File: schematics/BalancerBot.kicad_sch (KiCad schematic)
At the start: 7 parts, among them M1 Motor_DC, M2 Motor_DC, U1 MCP73871, U2 L298N

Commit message: Update
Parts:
- removed U2: L298N, Package_TO_SOT_THT:TO-220-15_P2.54x5.08mm_StaggerOdd_Lead4.58mm_Vertical, symbol Driver_Motor:L298N
- added Boost_5V: (no value), symbol 1MyLibrary:Power_Boost_module_-_5V_0.5A_JST
- added L9110S: (no value), symbol MyLibrary:L9110S
- added MPU6050: (no value), symbol 1MyLibrary:SEN-MPU6050
- renumbered U1 to BatteryManager
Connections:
- net at M2.1 (+): now also L9110S. (OUTA2)
- net at M2.2 (-): now also L9110S. (OUTA2)
- net at BatteryManager.14 (V_{BAT}), BatteryManager.15 (V_{BAT}): no longer BT1.1 (+)
- net at BT1.2 (-): now also Boost_5V. (Bat-)
- net at M1.1 (+): now also L9110S. (OUTA2)
- net at M1.2 (-): now also L9110S. (OUTA2)
- net GNDREF: now reaches A2.13 (GND), A2.18 (GND), A2.23 (GND), A2.28 (GND), A2.3 (GND), A2.38 (GND), A2.8 (GND)
- net GNDREF: now also Boost_5V. (Bat-), L9110S. (OUTA2), MPU6050. (GND)
- net at A2.21 (GPIO16): now also L9110S. (OUTA2)
- net at A2.22 (GPIO17): now also L9110S. (OUTA2)
- net at A2.24 (GPIO18): now also L9110S. (OUTA2)
- net at A2.25 (GPIO19): now also L9110S. (OUTA2)
- net at A2.26 (GPIO20): now also MPU6050. (GND)
- net at A2.27 (GPIO21): now also MPU6050. (GND)
- net at A2.36 (3V3): now also MPU6050. (GND)
- net at A2.39 (VSYS): now also Boost_5V. (Bat-), L9110S. (OUTA2)
- new net: BT1.1 (+), Boost_5V. (Bat-)
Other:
- note added: "ESP32 VIN = 6V/7.5V MOTORS(Vss) = 6V/7.5V RaspPico VSYS = 1.8-5.5V DC (no USB)"
- note added: "VBUS and VSYS must NOT be used simultaneously!"
- moved on the sheet: A1, A2, BT1, BatteryManager, M1, M2

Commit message: Update schematic
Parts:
- removed A1: Arduino_Nano_ESP32, Module:Arduino_Nano, symbol MCU_Module:Arduino_Nano_ESP32
- removed BatteryManager: MCP73871, Package_DFN_QFN:QFN-20-1EP_4x4mm_P0.5mm_EP2.5x2.5mm, symbol Battery_Management:MCP73871
- removed Boost_5V: (no value), symbol 1MyLibrary:Power_Boost_module_-_5V_0.5A_JST
- removed L9110S: (no value), symbol MyLibrary:L9110S
- removed M1, M2: Motor_DC, symbol Motor:Motor_DC
- added LED: Red, PCM_SparkFun-LED:LED_0402_1005Metric_Red, symbol PCM_SparkFun-LED:LED_Red_0402
- added M1, M2: Motor_Servo, symbol Motor:Motor_Servo
- added R1: 100ohm, symbol PCM_Resistor_AKL:R_Generic
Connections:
- net at MPU6050. (GND): now also A2.36 (3V3)
- net at BT1.1 (+): now also A2.39 (VSYS), M1.2 (+), M2.2 (+)
- net at BT1.2 (-): now also A2.13 (GND), A2.18 (GND), A2.23 (GND), A2.28 (GND), A2.3 (GND), A2.38 (GND), A2.8 (GND), MPU6050. (GND), LED.1 (K), M1.3 (-), M2.3 (-)
- net at A2.29 (GPIO22): now also R1.2
- net at A2.31 (GPIO26_ADC0): now also M1.1 (PWM)
- net at A2.32 (GPIO27_ADC1): now also M2.1 (PWM)
- removed net GNDREF: A2.13 (GND), A2.18 (GND), A2.23 (GND), A2.28 (GND), A2.3 (GND), A2.38 (GND), A2.8 (GND), MPU6050. (GND)
- new net: LED.2 (A), R1.1
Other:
- note added: "RaspPico VSYS = 1.8-5.5V DC (no USB)"
- note removed: "ESP32 VIN = 6V/7.5V MOTORS(Vss) = 6V/7.5V RaspPico VSYS = 1.8-5.5V DC (no USB)"
- moved on the sheet: A2, BT1, MPU6050

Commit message: 9dof IMU testing
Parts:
- added BT2: LiPo_Cell, symbol Device:Battery_Cell
- added D1: LED(G), symbol Device:LED
- added M3, M4: Motor_Servo, symbol Motor:Motor_Servo
- added R2: 220/110ohm, symbol PCM_Resistor_AKL:R_Generic
- added R3: 330ohm, symbol PCM_Resistor_AKL:R_Generic
- added SW1: SW_SPDT, symbol Switch:SW_SPDT
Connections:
- net at MPU6050. (GND): now also A2.36 (3V3)
- new net: BT2.1 (+), SW1.3 (C)
- new net: D1.2 (A), R2.2
- new net M1: M4.1 (PWM)
- new net M2: M3.1 (PWM)
- new net Pico GND: BT2.2 (-), D1.1 (K), M3.3 (-), M4.3 (-)
- new net Pico VSYS: M3.2 (+), M4.2 (+), R2.1, R3.2, SW1.2 (B)
- new net Voltage Measure: R3.1

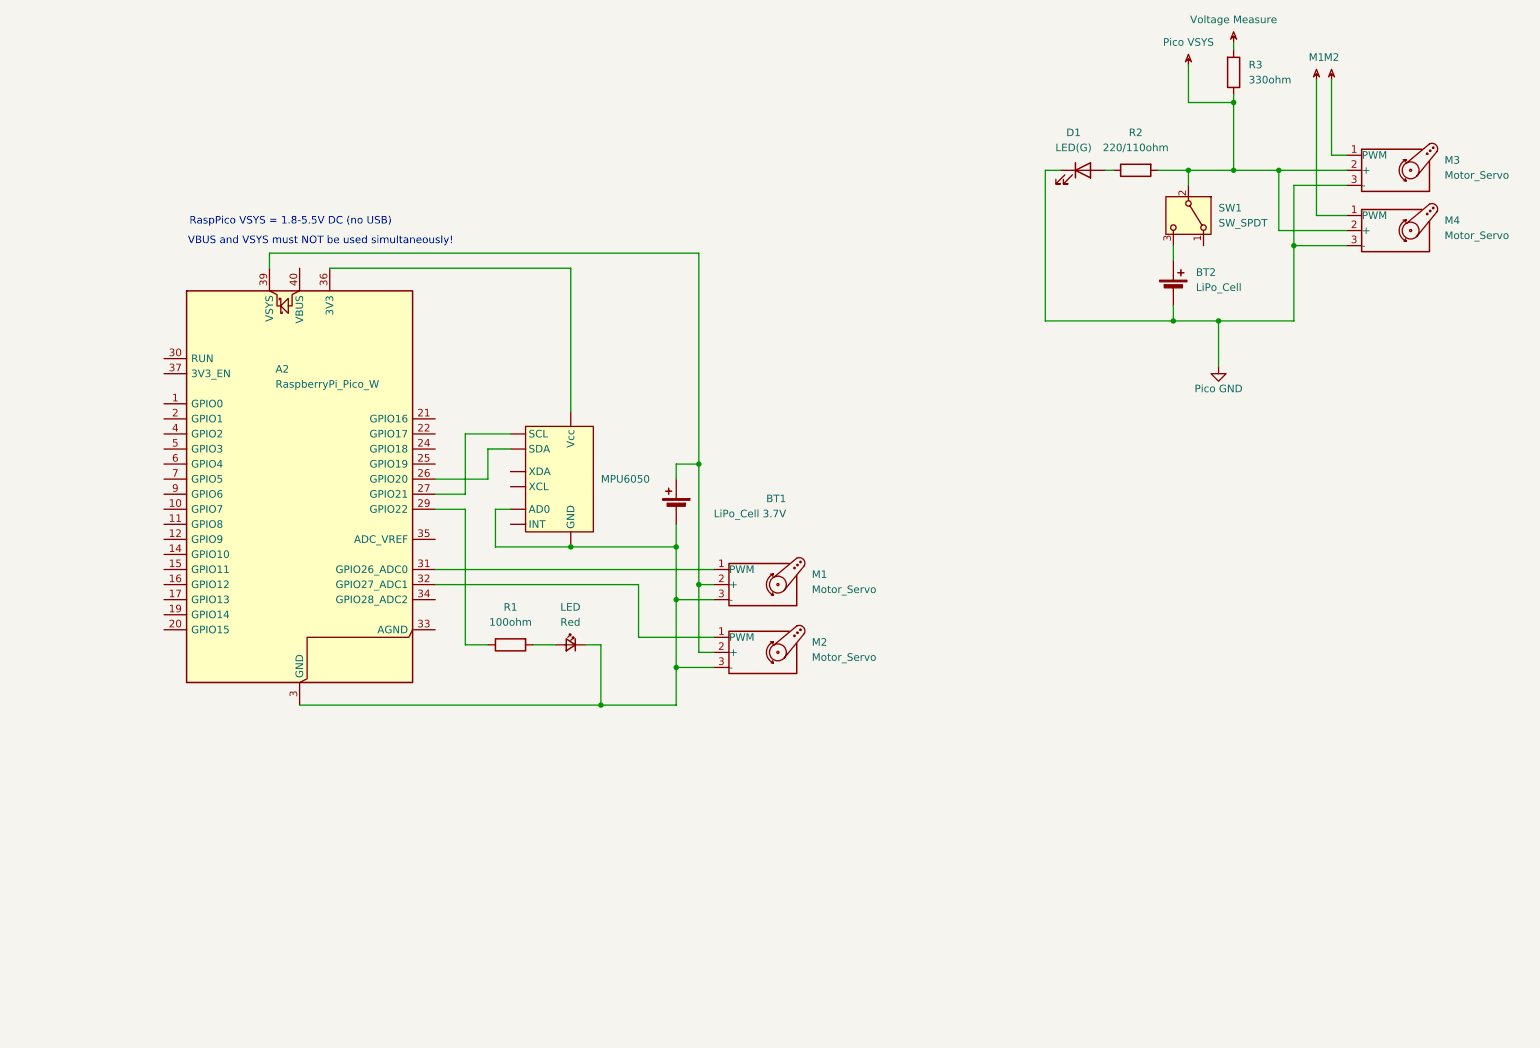
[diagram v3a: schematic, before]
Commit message: Driving and turning
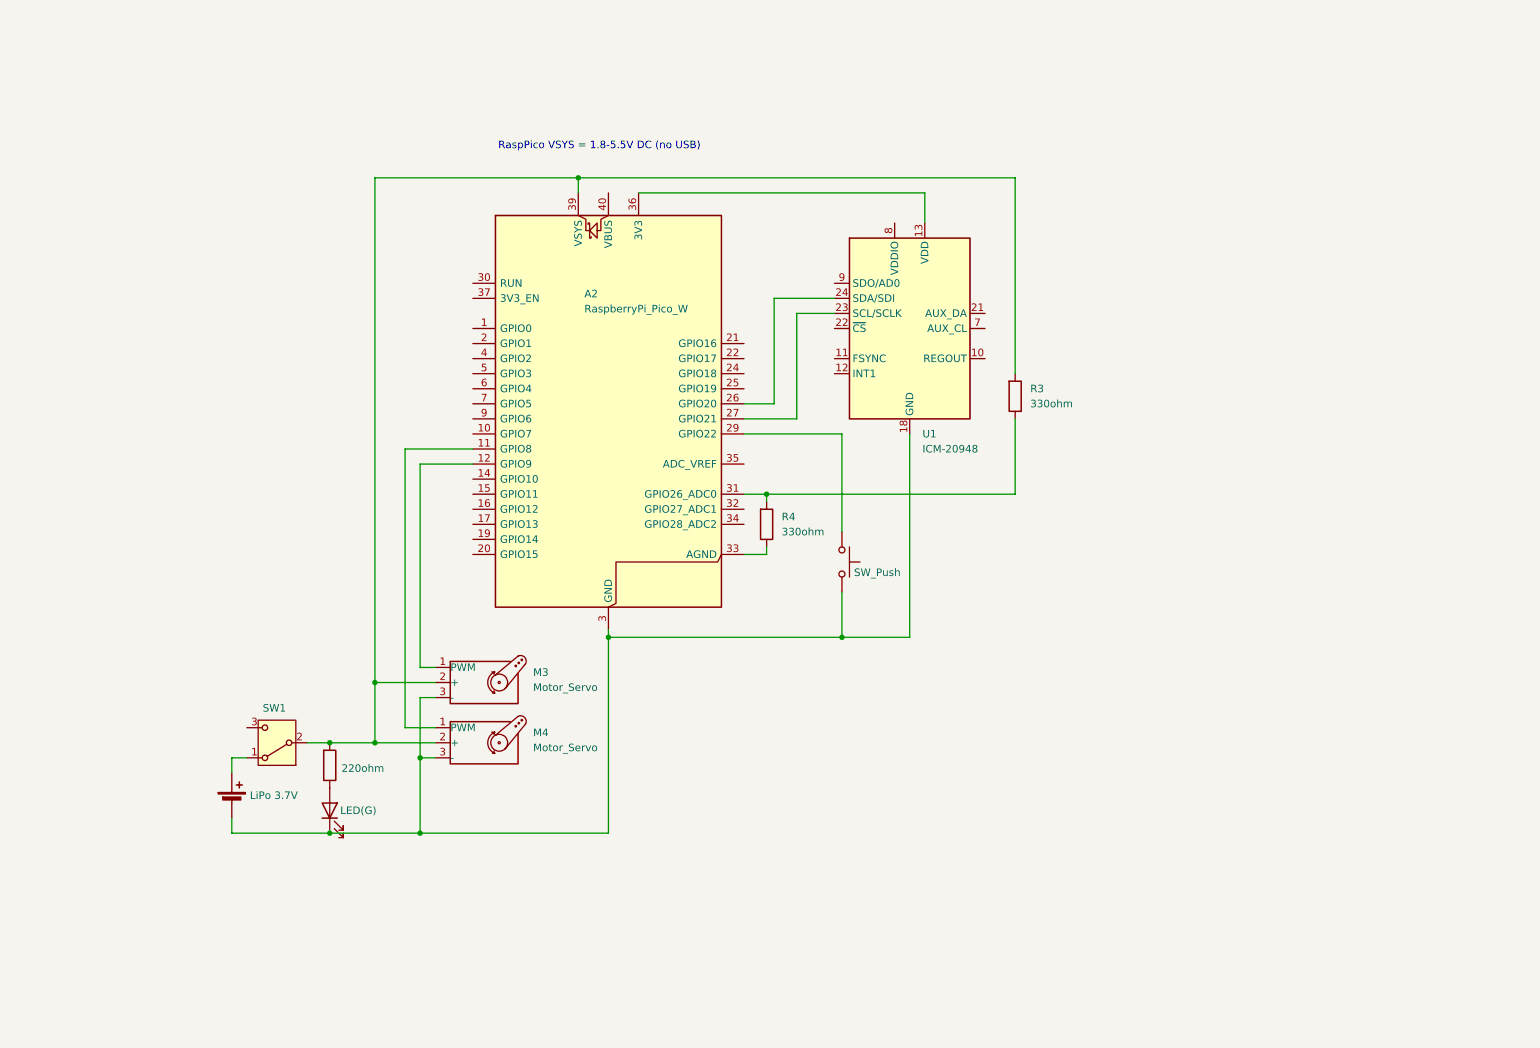
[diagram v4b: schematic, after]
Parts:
- removed BT1: LiPo_Cell 3.7V, symbol Device:Battery_Cell
- removed LED: Red, PCM_SparkFun-LED:LED_0402_1005Metric_Red, symbol PCM_SparkFun-LED:LED_Red_0402
- removed M1, M2: Motor_Servo, symbol Motor:Motor_Servo
- removed MPU6050: (no value), symbol 1MyLibrary:SEN-MPU6050
- removed R1: 100ohm, symbol PCM_Resistor_AKL:R_Generic
- added R4: 330ohm, symbol PCM_Resistor_AKL:R_Generic
- added SW2: SW_Push, symbol Switch:SW_Push
- added U1: ICM-20948, Sensor_Motion:InvenSense_QFN-24_3x3mm_P0.4mm, symbol Sensor_Motion:ICM-20948
- BT2: value LiPo_Cell -> LiPo 3.7V
- R2: value 220/110ohm -> 220ohm
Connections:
- net M1 is gone; now on an unnamed net: M4.1 (PWM)
- net M2 is gone; now on an unnamed net: M3.1 (PWM)
- net Pico GND is gone; now on an unnamed net: BT2.2 (-), D1.1 (K), M3.3 (-), M4.3 (-)
- net Voltage Measure is gone; now on an unnamed net: R3.1
- net at A2.13 (GND), A2.18 (GND), A2.23 (GND)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: now also SW2.2, U1.18 (GND), U1.20 (GND)
- net at SW1.1 (A): now also BT2.1 (+)
- net at SW1.3 (C): no longer BT2.1 (+)
- net at A2.29 (GPIO22): now also SW2.1
- net at A2.26 (GPIO20): now also U1.24 (SDA/SDI)
- net at A2.27 (GPIO21): now also U1.23 (SCL/SCLK)
- net at A2.36 (3V3): now also U1.13 (VDD)
- net at A2.39 (VSYS): now also M3.2 (+), M4.2 (+), R2.1, SW1.2 (B)
- net at A2.31 (GPIO26_ADC0): now also R3.2, R4.1
- net at A2.33 (AGND): now also R4.2
- removed net Pico VSYS: M3.2 (+), M4.2 (+), R2.1, R3.2, SW1.2 (B)
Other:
- note removed: "VBUS and VSYS must NOT be used simultaneously!"
- moved on the sheet: A2, M3, M4, R3, SW1

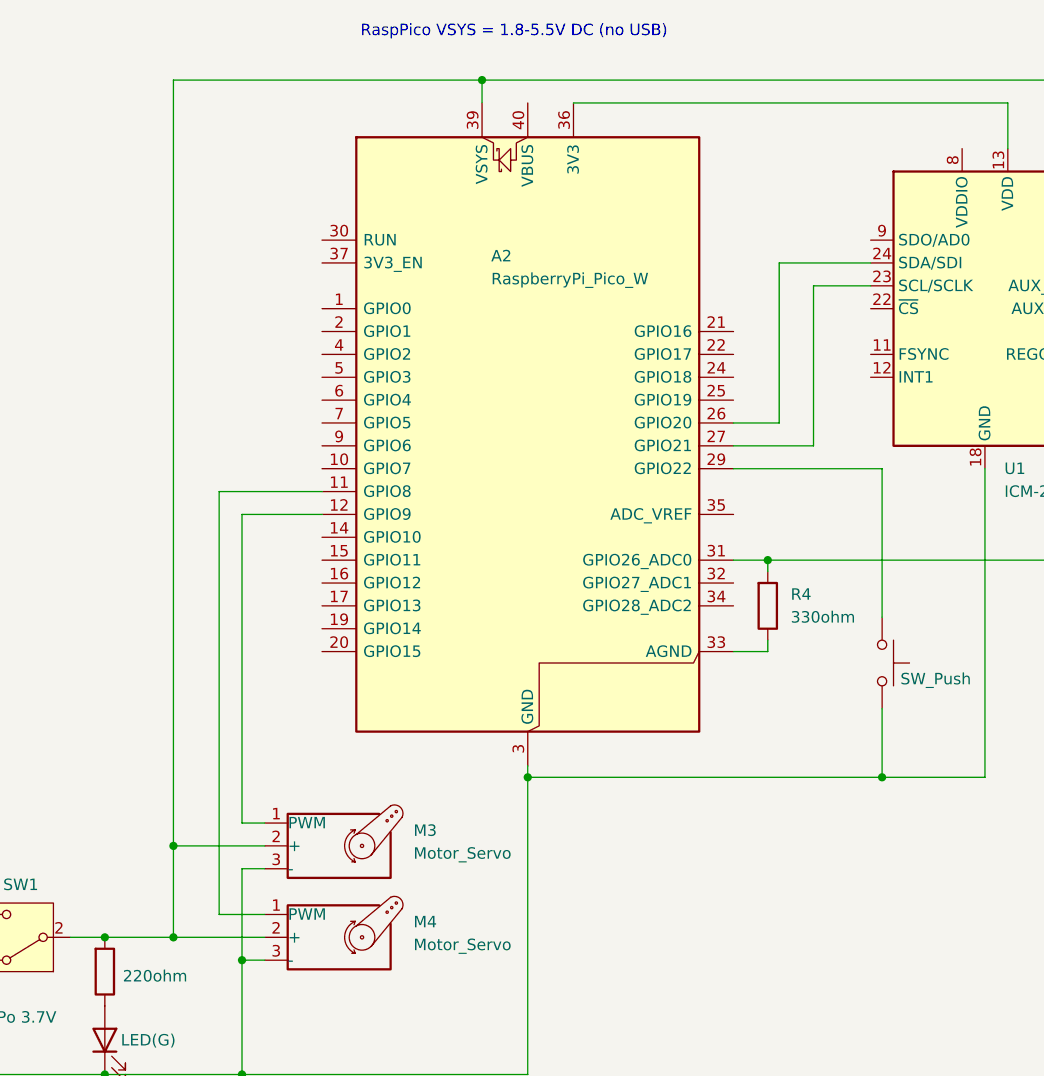
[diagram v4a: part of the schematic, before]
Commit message: 8x8 ToF sensor testing
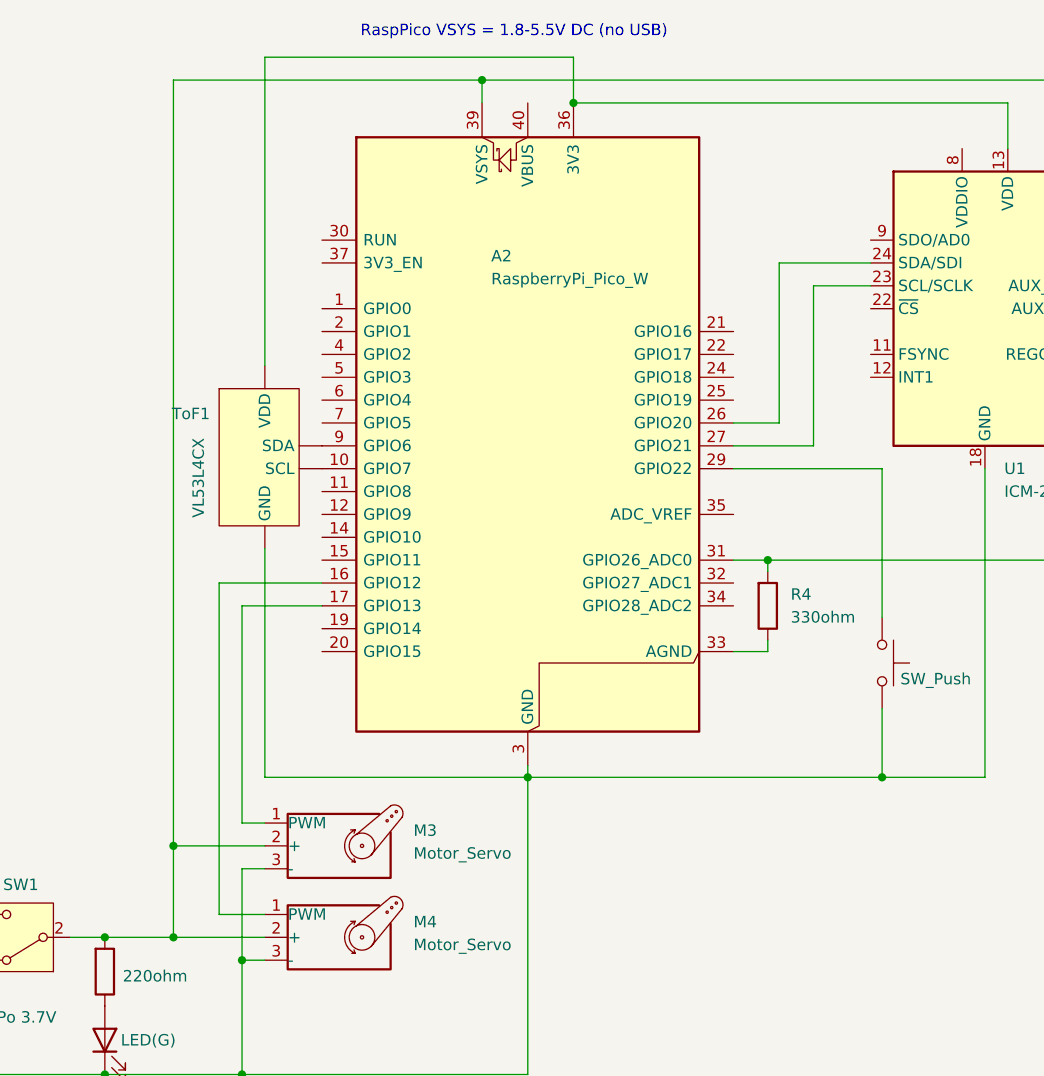
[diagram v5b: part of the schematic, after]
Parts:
- added ToF1: VL53L4CX, symbol 1MyLibrary:VL53L4CX
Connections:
- net at A2.36 (3V3), U1.13 (VDD): now also ToF1. (SCL)
- net at A2.13 (GND), A2.18 (GND), A2.23 (GND)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: now also ToF1. (SCL)
- net at M4.1 (PWM): now also A2.16 (GPIO12); no longer A2.11 (GPIO8)
- net at M3.1 (PWM): now also A2.17 (GPIO13); no longer A2.12 (GPIO9)
- net at A2.10 (GPIO7): now also ToF1. (SCL)
- net at A2.9 (GPIO6): now also ToF1. (SCL)
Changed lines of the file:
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@@
+	)
+	(junction
+		(at 129.54 52.07)
+		(diameter 0)
+		(color 0 0 0 0)
 	)
 	(junction
@@
 	(wire
 		(pts
+			(xy 95.25 81.28) (xy 95.25 46.99)
+		)
+		(stroke
+			(width 0)
+			(type default)
+		)
+	)
+	(wire
+		(pts
 			(xy 60.96 160.02) (xy 77.47 160.02)
 		)
@@
 	(wire
 		(pts
+			(xy 129.54 46.99) (xy 129.54 52.07)
+		)
+		(stroke
+			(width 0)
+			(type default)
+		)
+	)
+	(wire
+		(pts
 			(xy 92.71 160.02) (xy 124.46 160.02)
 		)
@@
 	(wire
 		(pts
-			(xy 101.6 97.79) (xy 92.71 97.79)
-		)
-		(stroke
-			(width 0)
-			(type default)
-		)
-	)
-	(wire
-		(pts
 			(xy 95.25 137.16) (xy 92.71 137.16)
 		)
@@
 	(wire
 		(pts
+			(xy 90.17 105.41) (xy 90.17 142.24)
+		)
+		(stroke
+			(width 0)
+			(type default)
+		)
+	)
+	(wire
+		(pts
 			(xy 151.13 102.87) (xy 193.04 102.87)
 		)
@@
 	(wire
 		(pts
+			(xy 90.17 105.41) (xy 101.6 105.41)
+		)
+		(stroke
+			(width 0)
+			(type default)
+		)
+	)
+	(wire
+		(pts
 			(xy 124.46 127) (xy 124.46 160.02)
 		)
@@
 	(wire
 		(pts
-			(xy 101.6 95.25) (xy 90.17 95.25)
+			(xy 92.71 107.95) (xy 92.71 132.08)
 		)
 		(stroke
@@
 	(wire
 		(pts
-			(xy 92.71 97.79) (xy 92.71 132.08)
-		)
-		(stroke
-			(width 0)
-			(type default)
-		)
-	)
-	(wire
-		(pts
 			(xy 77.47 160.02) (xy 92.71 160.02)
 		)
@@
 	(wire
 		(pts
+			(xy 92.71 107.95) (xy 101.6 107.95)
+		)
+		(stroke
+			(width 0)
+			(type default)
+		)
+	)
+	(wire
+		(pts
 			(xy 151.13 102.87) (xy 151.13 104.14)
 		)
@@
 	(wire
 		(pts
-			(xy 90.17 95.25) (xy 90.17 142.24)
+			(xy 95.25 101.6) (xy 95.25 127)
 		)
 		(stroke
@@
 	(wire
 		(pts
-			(xy 163.83 127) (xy 124.46 127)
-		)
-		(stroke
-			(width 0)
-			(type default)
-		)
-	)
-	(wire
-		(pts
 			(xy 163.83 92.71) (xy 163.83 109.22)
 		)
@@
 	(wire
 		(pts
+			(xy 95.25 46.99) (xy 129.54 46.99)
+		)
+		(stroke
+			(width 0)
+			(type default)
+		)
+	)
+	(wire
+		(pts
 			(xy 92.71 137.16) (xy 92.71 147.32)
 		)
@@
 		(pts
 			(xy 60.96 147.32) (xy 63.5 147.32)
+		)
+		(stroke
+			(width 0)
+			(type default)
+		)
+	)
+	(wire
+		(pts
+			(xy 95.25 127) (xy 163.83 127)
 		)
 		(stroke
@@
 					(unit 1)
 				)
+			)
+		)
+	)
+	(symbol
+		(lib_id "1MyLibrary:VL53L4CX")
+		(at 93.98 82.55 0)
+		(unit 1)
+		(body_style 1)
+		(exclude_from_sim no)
+		(in_bom yes)
+		(on_board yes)
+		(in_pos_files yes)
+		(dnp no)
+		(property "Reference" "ToF1"
+			(at 89.154 86.614 0)
+			(show_name no)
+			(do_not_autoplace no)
+			(effects
+				(font
+					(size 1.27 1.27)
+				)
+				(justify right)
+			)
+		)
+		(property "Value" "VL53L4CX"
+			(at 87.884 93.726 90)
+			(show_name no)
+			(do_not_autoplace no)
+			(effects
+				(font
+					(size 1.27 1.27)
+				)
+			)
+		)
+		(property "Footprint" ""
+			(at 93.98 82.55 0)
+			(hide yes)
+			(show_name no)
+			(do_not_autoplace no)
+			(effects
+				(font
+					(size 1.27 1.27)
+				)
+			)
+		)
+		(property "Datasheet" ""
+			(at 93.98 82.55 0)
+			(hide yes)
+			(show_name no)
+			(do_not_autoplace no)
+			(effects
+				(font
+					(size 1.27 1.27)
+				)
+			)
+		)
+		(property "Description" ""
+			(at 93.98 82.55 0)
+			(hide yes)
+			(show_name no)
+			(do_not_autoplace no)
+			(effects
+				(font
+					(size 1.27 1.27)
+				)
+			)
+		)
+		(pin ""
+		)
+		(pin ""
+		)
+		(pin ""
+		)
+		(pin ""
+		)
+		(instances
+			(project "BalancerBot"
+				(path "/6fa14e48-cd8a-4639-b9f0-f8e9e08c6d97"
+					(reference "ToF1")
+					(unit 1)
+				)
